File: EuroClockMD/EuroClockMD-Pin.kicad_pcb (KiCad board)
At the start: 2 copper layers, 29 x 106 mm, 13 parts, among them J5 EURO_PWR_2x5, J6 Conn_01x15_Pin_Left, J9 Conn_01x15_Pin_Right

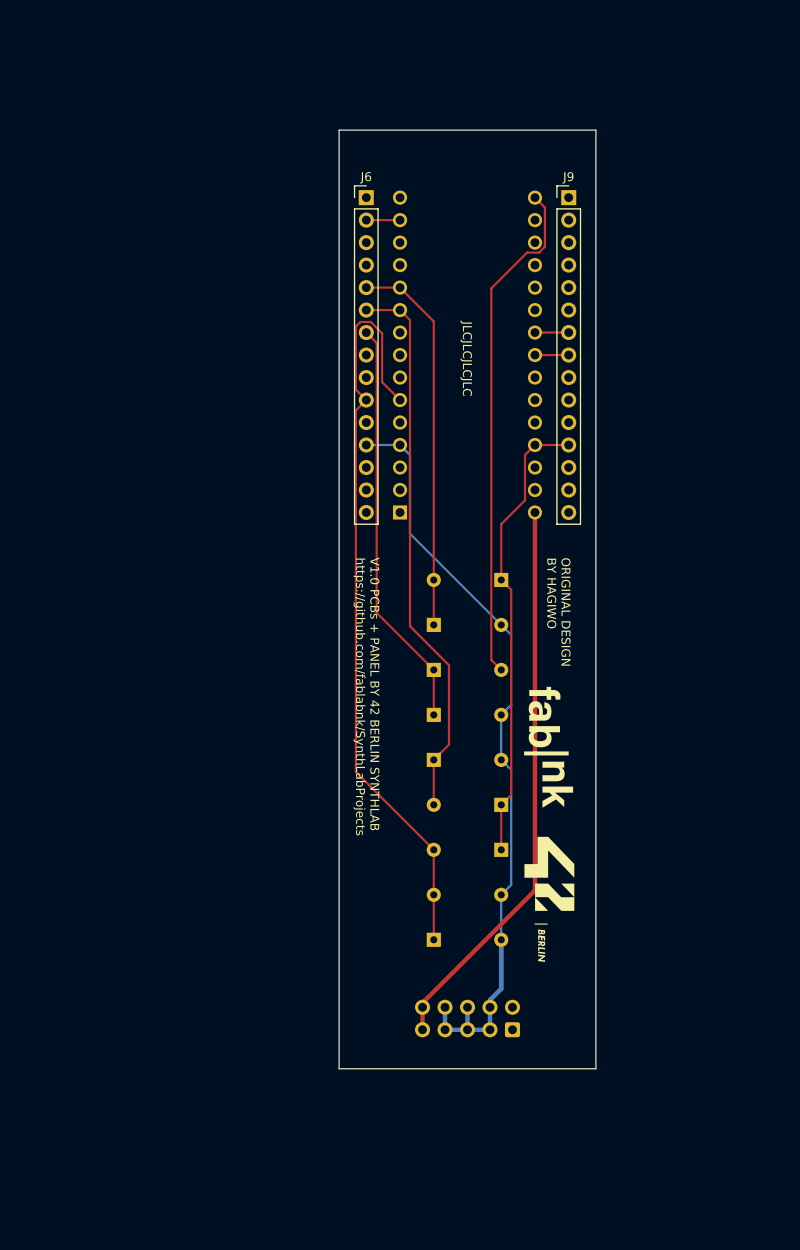
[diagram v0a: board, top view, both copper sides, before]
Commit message: retraced EuroClockMD-Pin and moved holes in EuroClockMD-panel
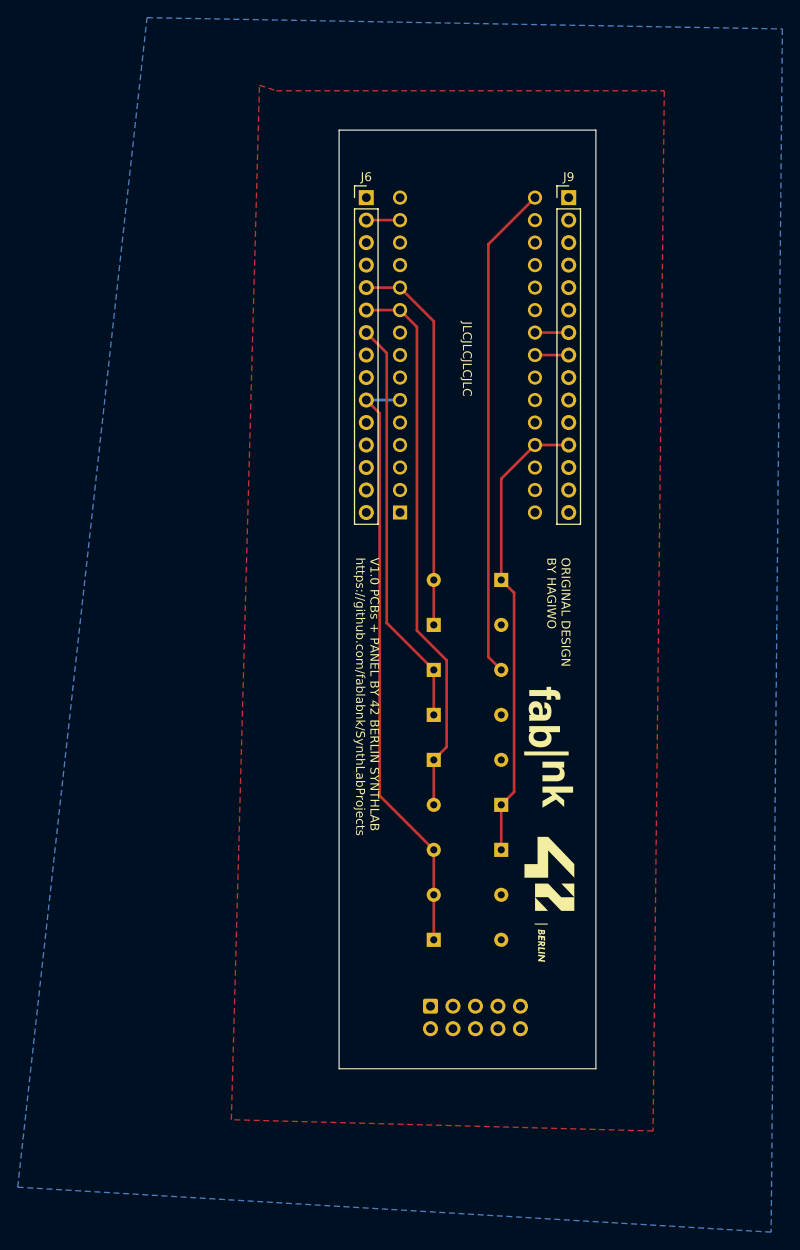
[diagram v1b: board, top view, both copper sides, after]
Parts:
- J5: footprint Connector_IDC:IDC-Header_2x05_P2.54mm_Vertical -> 4ms_Connector:Pins_2x05_2.54mm_TH_EurorackPower_Shrouded
- moved J5 6.09 mm to (181.2, 138.3), turned to 90 degrees
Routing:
- net GND: track 87.1 -> 0.00 mm
- net Net-(A1-VIN): track 63.7 -> 0.00 mm
- net P3: track 86.0 -> 67.9 mm
- net Net-(A1-D13): track 57.6 -> 56.1 mm
- added copper zone on B.Cu, net GND
- added copper zone on F.Cu, net Net-(A1-VIN)
